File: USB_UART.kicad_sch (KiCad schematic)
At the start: 10 parts, among them J3 USB Type C Connector, U5 FT232RL

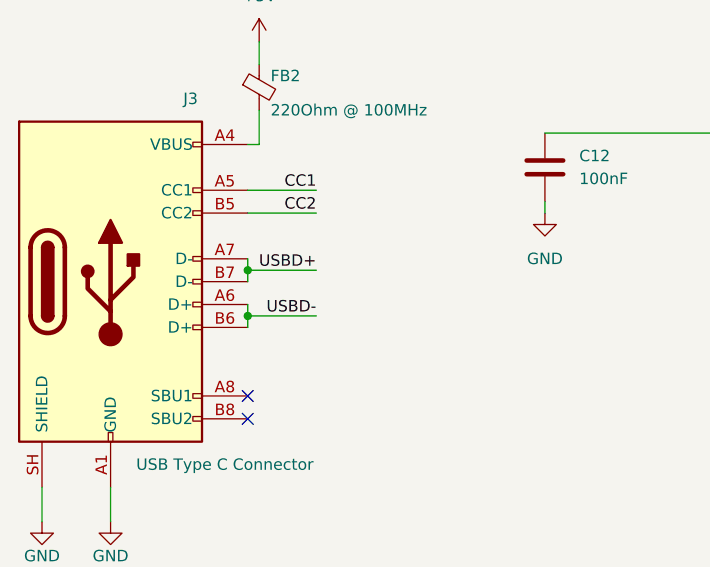
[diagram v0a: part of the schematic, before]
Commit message: fix(usb): correct D+/D- routing between J3 and U5
USB data lines were swapped at the Type-C receptacle.
J3 D+ now routes to U5 USBD+ and J3 D- to U5 USBD-.
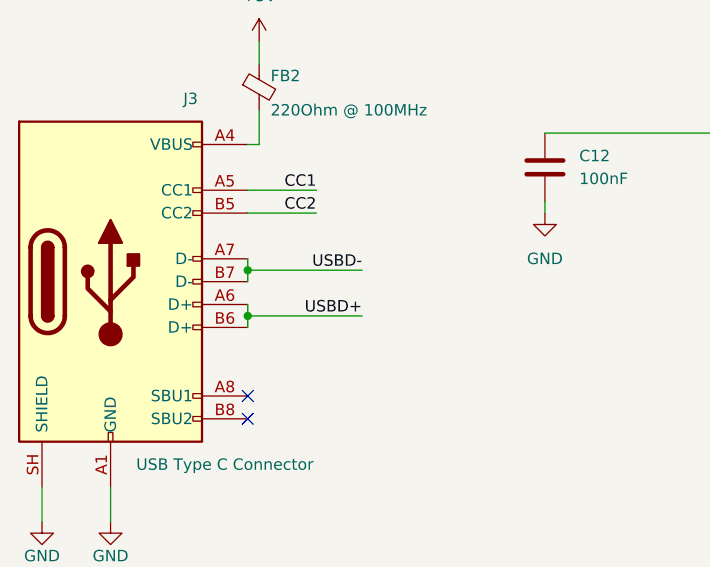
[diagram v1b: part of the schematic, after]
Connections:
- net USBD+: now also J3.A6 (D+), J3.B6 (D+); no longer J3.A7 (D-), J3.B7 (D-)
- net USBD-: now also J3.A7 (D-), J3.B7 (D-); no longer J3.A6 (D+), J3.B6 (D+)
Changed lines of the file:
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@@
+	)
+	(junction
+		(at 204.47 134.62)
+		(diameter 0)
+		(color 0 0 0 0)
 	)
 	(junction
@@
 		(color 0 0 0 0)
 	)
-	(junction
-		(at 204.47 134.62)
-		(diameter 0)
-		(color 0 0 0 0)
-	)
 	(no_connect
 		(at 222.25 101.6)
@@
 	(wire
 		(pts
-			(xy 110.49 106.68) (xy 118.11 106.68)
+			(xy 123.19 111.76) (xy 110.49 111.76)
 		)
 		(stroke
@@
 	(wire
 		(pts
-			(xy 110.49 111.76) (xy 118.11 111.76)
+			(xy 110.49 106.68) (xy 110.49 107.95)
 		)
 		(stroke
@@
 	(wire
 		(pts
+			(xy 110.49 111.76) (xy 110.49 113.03)
+		)
+		(stroke
+			(width 0)
+			(type default)
+		)
+	)
+	(wire
+		(pts
 			(xy 213.36 20.32) (xy 213.36 22.86)
 		)
@@
 	(wire
 		(pts
-			(xy 110.49 111.76) (xy 110.49 113.03)
+			(xy 110.49 110.49) (xy 110.49 111.76)
 		)
 		(stroke
@@
 		(pts
 			(xy 204.47 78.74) (xy 204.47 83.82)
+		)
+		(stroke
+			(width 0)
+			(type default)
+		)
+	)
+	(wire
+		(pts
+			(xy 123.19 106.68) (xy 110.49 106.68)
 		)
 		(stroke
@@
 	(wire
 		(pts
-			(xy 110.49 106.68) (xy 110.49 107.95)
-		)
-		(stroke
-			(width 0)
-			(type default)
-		)
-	)
-	(wire
-		(pts
 			(xy 110.49 92.71) (xy 111.76 92.71)
 		)
@@
 		(pts
 			(xy 111.76 81.28) (xy 111.76 83.82)
-		)
-		(stroke
-			(width 0)
-			(type default)
-		)
-	)
-	(wire
-		(pts
-			(xy 110.49 110.49) (xy 110.49 111.76)
 		)
 		(stroke
@@
 		)
 	)
+	(label "USBD+"
+		(at 123.19 111.76 180)
+		(effects
+			(font
+				(size 1.27 1.27)
+			)
+			(justify right bottom)
+		)
+	)
 	(label "CC2"
 		(at 274.32 16.51 0)
@@
 		)
 	)
-	(label "USBD+"
-		(at 118.11 106.68 180)
-		(effects
-			(font
-				(size 1.27 1.27)
-			)
-			(justify right bottom)
-		)
-	)
 	(label "CC1"
 		(at 118.11 97.79 180)
@@
 		)
 	)
-	(label "USBD-"
-		(at 118.11 111.76 180)
-		(effects
-			(font
-				(size 1.27 1.27)
-			)
-			(justify right bottom)
-		)
-	)
 	(label "CC2"
 		(at 118.11 100.33 180)
 		(effects
 			(font
+				(size 1.27 1.27)
+			)
+			(justify right bottom)
+		)
+	)
+	(label "USBD-"
+		(at 123.19 106.68 180)
+		(effects
+			(font

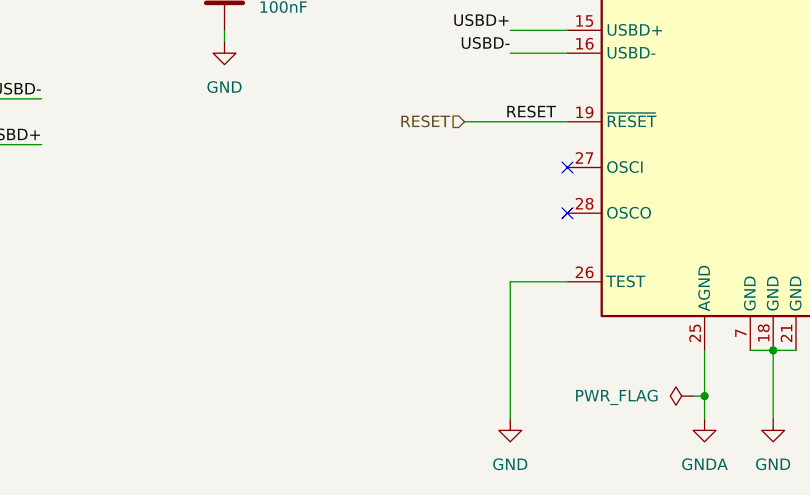
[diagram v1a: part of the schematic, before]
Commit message: fix(usb-uart): add 12MHz crystal oscillator for FT232RL
FT232RL OSCI/OSCO were unconnected, leaving the USB-UART bridge
without its mandatory 12MHz clock so USB would never enumerate.
Adds Y1 12MHz crystal with 27pF load caps C13/C14 to GND, wired
OSCI to Y1.1 and OSCO to Y1.2.
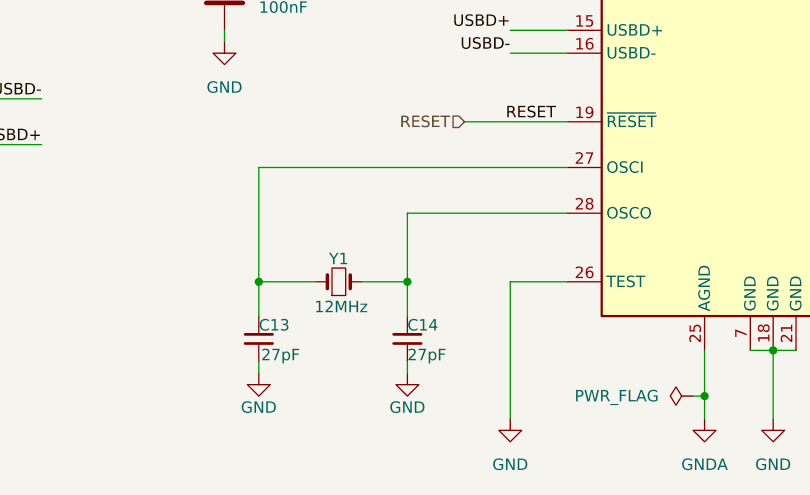
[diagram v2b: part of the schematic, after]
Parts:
- added C13, C14: 27pF, PCM_SparkFun-Capacitor:C_0603_1608Metric, symbol Device:C_Small
- added Y1: 12MHz, Crystal:Crystal_SMD_0603-2Pin_6.0x3.5mm_HandSoldering, symbol PCM_SparkFun-Clock:Crystal
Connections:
- net GND: now also C13.2, C14.2
- net at U5.27 (OSCI): now also C13.1, Y1.1
- net at U5.28 (OSCO): now also C14.1, Y1.2
- no-connect marks 13 -> 11
